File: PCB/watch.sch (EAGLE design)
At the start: 47 parts, among them IC1 ISL1209, J2 USB-MICROB, T1 BC850, U2 MKL27Z256VLH4

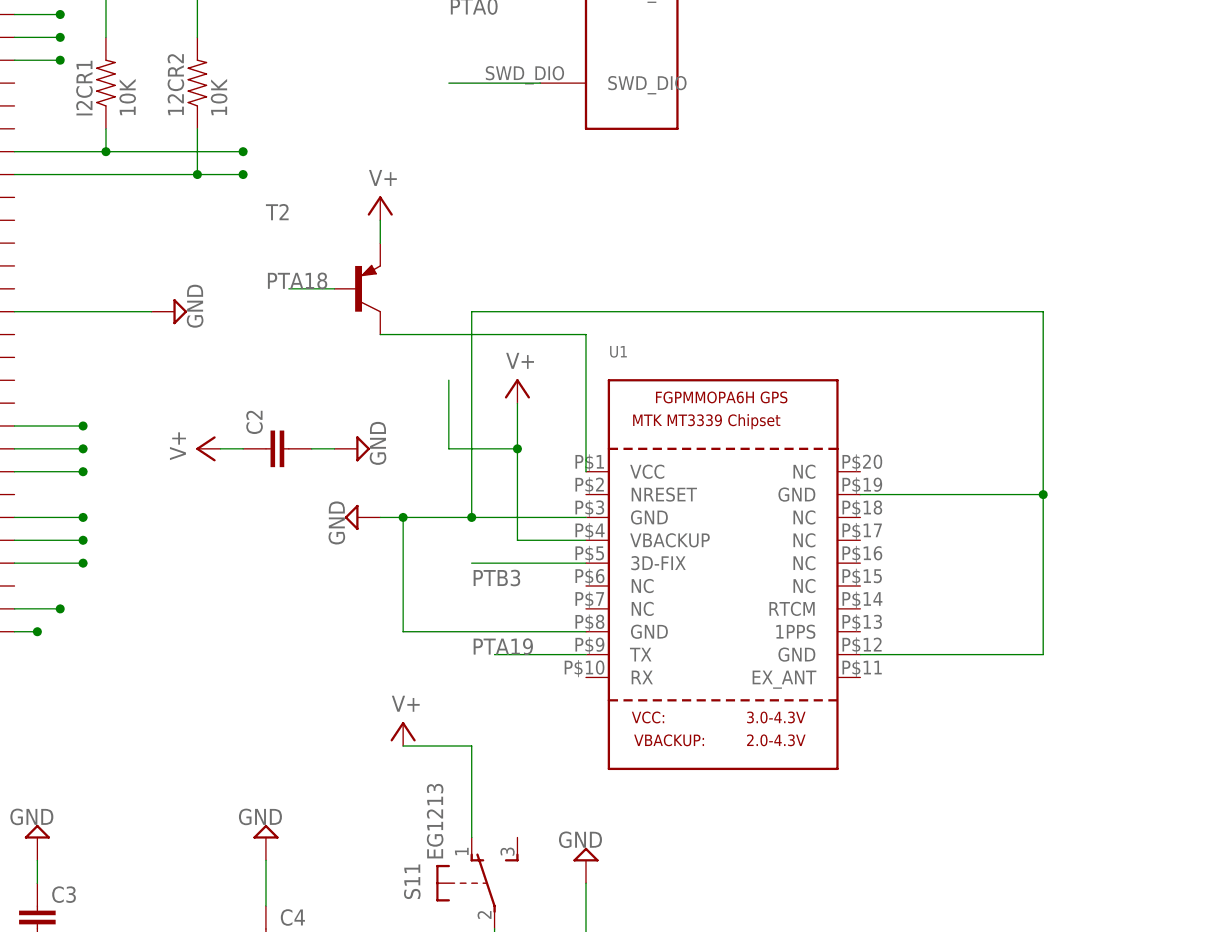
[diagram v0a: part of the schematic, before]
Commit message: cleaned up gps, added label for gps cap
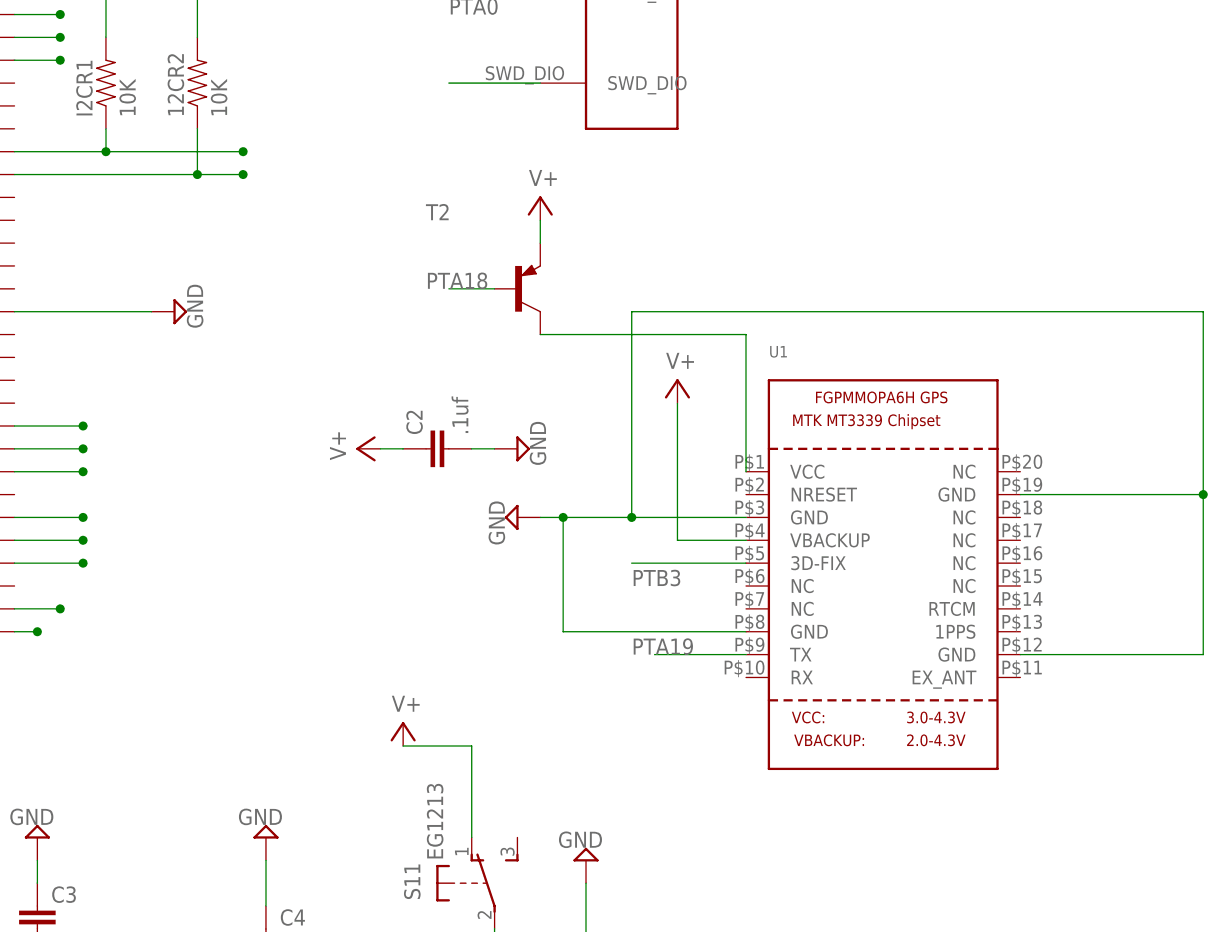
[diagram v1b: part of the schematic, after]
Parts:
- C2: value (none) -> .1uf
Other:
- moved on the sheet: C2, T2, U1
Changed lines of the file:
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@@
 <part name="SUPPLY6" library="supply2" deviceset="GND" device=""/>
 <part name="SUPPLY7" library="supply2" deviceset="GND" device=""/>
-<part name="C2" library="SparkFun" deviceset="CAP" device="0603"/>
+<part name="C2" library="SparkFun" deviceset="CAP" device="0603" value=".1uf"/>
 <part name="SUPPLY8" library="supply2" deviceset="V+" device=""/>
 <part name="SUPPLY9" library="supply2" deviceset="GND" device=""/>
@@
 <instance part="SUPPLY3" gate="1" x="-63.5" y="71.12"/>
 <instance part="SUPPLY4" gate="GND" x="58.42" y="55.88" rot="R90"/>
-<instance part="U1" gate="G$1" x="160.02" y="91.44"/>
-<instance part="SUPPLY5" gate="GND" x="119.38" y="96.52" rot="R270"/>
+<instance part="U1" gate="G$1" x="177.8" y="91.44"/>
+<instance part="SUPPLY5" gate="GND" x="137.16" y="96.52" rot="R270"/>
 <instance part="U2" gate="A" x="-25.4" y="162.56"/>
 <instance part="SUPPLY6" gate="GND" x="-53.34" y="86.36" rot="R270"/>
 <instance part="SUPPLY7" gate="GND" x="99.06" y="119.38" rot="R90"/>
-<instance part="C2" gate="G$1" x="111.76" y="104.14" rot="R90"/>
-<instance part="SUPPLY8" gate="1" x="101.6" y="104.14" rot="R90"/>
-<instance part="SUPPLY9" gate="GND" x="119.38" y="104.14" rot="R90"/>
-<instance part="SUPPLY10" gate="1" x="137.16" y="111.76"/>
+<instance part="C2" gate="G$1" x="129.54" y="104.14" rot="R90"/>
+<instance part="SUPPLY8" gate="1" x="119.38" y="104.14" rot="R90"/>
+<instance part="SUPPLY9" gate="GND" x="137.16" y="104.14" rot="R90"/>
+<instance part="SUPPLY10" gate="1" x="154.94" y="111.76"/>
 <instance part="U$3" gate="G$1" x="25.4" y="63.5"/>
 <instance part="SP1" gate="S1" x="-81.28" y="109.22" rot="R270"/>
@@
 <instance part="SUPPLY31" gate="GND" x="-129.54" y="165.1"/>
 <instance part="R17" gate="G$1" x="-152.4" y="177.8"/>
-<instance part="T2" gate="G$1" x="119.38" y="121.92"/>
-<instance part="SUPPLY32" gate="1" x="121.92" y="132.08"/>
+<instance part="T2" gate="G$1" x="137.16" y="121.92"/>
+<instance part="SUPPLY32" gate="1" x="139.7" y="132.08"/>
 </instances>
 <busses>
@@
 <pinref part="U1" gate="G$1" pin="GND@1"/>
 <pinref part="SUPPLY5" gate="GND" pin="GND"/>
-<wire x1="144.78" y1="96.52" x2="132.08" y2="96.52" width="0.1524" layer="91"/>
+<wire x1="162.56" y1="96.52" x2="149.86" y2="96.52" width="0.1524" layer="91"/>
 <pinref part="U1" gate="G$1" pin="GND@3"/>
-<wire x1="132.08" y1="96.52" x2="124.46" y2="96.52" width="0.1524" layer="91"/>
-<wire x1="124.46" y1="96.52" x2="121.92" y2="96.52" width="0.1524" layer="91"/>
-<wire x1="175.26" y1="81.28" x2="195.58" y2="81.28" width="0.1524" layer="91"/>
-<wire x1="195.58" y1="81.28" x2="195.58" y2="99.06" width="0.1524" layer="91"/>
-<wire x1="195.58" y1="99.06" x2="195.58" y2="119.38" width="0.1524" layer="91"/>
-<wire x1="195.58" y1="119.38" x2="132.08" y2="119.38" width="0.1524" layer="91"/>
-<wire x1="132.08" y1="119.38" x2="132.08" y2="96.52" width="0.1524" layer="91"/>
-<junction x="132.08" y="96.52"/>
+<wire x1="149.86" y1="96.52" x2="142.24" y2="96.52" width="0.1524" layer="91"/>
+<wire x1="142.24" y1="96.52" x2="139.7" y2="96.52" width="0.1524" layer="91"/>
+<wire x1="193.04" y1="81.28" x2="213.36" y2="81.28" width="0.1524" layer="91"/>
+<wire x1="213.36" y1="81.28" x2="213.36" y2="99.06" width="0.1524" layer="91"/>
+<wire x1="213.36" y1="99.06" x2="213.36" y2="119.38" width="0.1524" layer="91"/>
+<wire x1="213.36" y1="119.38" x2="149.86" y2="119.38" width="0.1524" layer="91"/>
+<wire x1="149.86" y1="119.38" x2="149.86" y2="96.52" width="0.1524" layer="91"/>
+<junction x="149.86" y="96.52"/>
 <pinref part="U1" gate="G$1" pin="GND@4"/>
-<wire x1="175.26" y1="99.06" x2="195.58" y2="99.06" width="0.1524" layer="91"/>
-<junction x="195.58" y="99.06"/>
+<wire x1="193.04" y1="99.06" x2="213.36" y2="99.06" width="0.1524" layer="91"/>
+<junction x="213.36" y="99.06"/>
 <pinref part="U1" gate="G$1" pin="GND@2"/>
-<wire x1="144.78" y1="83.82" x2="124.46" y2="83.82" width="0.1524" layer="91"/>
-<wire x1="124.46" y1="83.82" x2="124.46" y2="96.52" width="0.1524" layer="91"/>
-<junction x="124.46" y="96.52"/>
+<wire x1="162.56" y1="83.82" x2="142.24" y2="83.82" width="0.1524" layer="91"/>
+<wire x1="142.24" y1="83.82" x2="142.24" y2="96.52" width="0.1524" layer="91"/>
+<junction x="142.24" y="96.52"/>
 </segment>
 <segment>
 <pinref part="C2" gate="G$1" pin="2"/>
 <pinref part="SUPPLY9" gate="GND" pin="GND"/>
-<wire x1="114.3" y1="104.14" x2="116.84" y2="104.14" width="0.1524" layer="91"/>
+<wire x1="132.08" y1="104.14" x2="134.62" y2="104.14" width="0.1524" layer="91"/>
 </segment>
 <segment>
@@
 <pinref part="SUPPLY8" gate="1" pin="V+"/>
 <pinref part="C2" gate="G$1" pin="1"/>
-<wire x1="104.14" y1="104.14" x2="106.68" y2="104.14" width="0.1524" layer="91"/>
+<wire x1="121.92" y1="104.14" x2="124.46" y2="104.14" width="0.1524" layer="91"/>
 </segment>
 <segment>
 <pinref part="SUPPLY10" gate="1" pin="V+"/>
 <pinref part="U1" gate="G$1" pin="VBACKUP"/>
-<wire x1="144.78" y1="93.98" x2="137.16" y2="93.98" width="0.1524" layer="91"/>
-<wire x1="137.16" y1="93.98" x2="137.16" y2="104.14" width="0.1524" layer="91"/>
-<wire x1="137.16" y1="104.14" x2="137.16" y2="109.22" width="0.1524" layer="91"/>
-<wire x1="129.54" y1="111.76" x2="129.54" y2="104.14" width="0.1524" layer="91"/>
-<wire x1="129.54" y1="104.14" x2="137.16" y2="104.14" width="0.1524" layer="91"/>
-<junction x="137.16" y="104.14"/>
+<wire x1="162.56" y1="93.98" x2="154.94" y2="93.98" width="0.1524" layer="91"/>
+<wire x1="154.94" y1="93.98" x2="154.94" y2="109.22" width="0.1524" layer="91"/>
 </segment>
 <segment>
@@
 <pinref part="SUPPLY32" gate="1" pin="V+"/>
 <pinref part="T2" gate="G$1" pin="E"/>
-<wire x1="121.92" y1="129.54" x2="121.92" y2="127" width="0.1524" layer="91"/>
+<wire x1="139.7" y1="129.54" x2="139.7" y2="127" width="0.1524" layer="91"/>
 </segment>
 </net>
@@
 <segment>
 <pinref part="U1" gate="G$1" pin="TX"/>
-<wire x1="144.78" y1="81.28" x2="134.62" y2="81.28" width="0.1524" layer="91"/>
-<label x="132.08" y="81.28" size="1.778" layer="95"/>
+<wire x1="162.56" y1="81.28" x2="152.4" y2="81.28" width="0.1524" layer="91"/>
+<label x="149.86" y="81.28" size="1.778" layer="95"/>
 </segment>
 </net>
@@
 <segment>
 <pinref part="U1" gate="G$1" pin="VCC"/>
-<wire x1="144.78" y1="101.6" x2="144.78" y2="116.84" width="0.1524" layer="91"/>
-<wire x1="144.78" y1="116.84" x2="121.92" y2="116.84" width="0.1524" layer="91"/>
+<wire x1="162.56" y1="101.6" x2="162.56" y2="116.84" width="0.1524" layer="91"/>
+<wire x1="162.56" y1="116.84" x2="139.7" y2="116.84" width="0.1524" layer="91"/>
 <pinref part="T2" gate="G$1" pin="C"/>
 </segment>
@@
 <segment>
 <pinref part="U1" gate="G$1" pin="3D-FIX"/>
-<wire x1="144.78" y1="91.44" x2="132.08" y2="91.44" width="0.1524" layer="91"/>
-<label x="132.08" y="88.9" size="1.778" layer="95"/>
+<wire x1="162.56" y1="91.44" x2="149.86" y2="91.44" width="0.1524" layer="91"/>
+<label x="149.86" y="88.9" size="1.778" layer="95"/>
 </segment>
 </net>
@@
 <segment>
 <pinref part="T2" gate="G$1" pin="B"/>
-<wire x1="116.84" y1="121.92" x2="111.76" y2="121.92" width="0.1524" layer="91"/>
-<label x="109.22" y="121.92" size="1.778" layer="95"/>
-</segment>
-</net>
+<wire x1="134.62" y1="121.92" x2="129.54" y2="121.92" width="0.1524" layer="91"/>
+<label x="127" y="121.92" size="1.778" layer="95"/>
+</segment>
+</net>

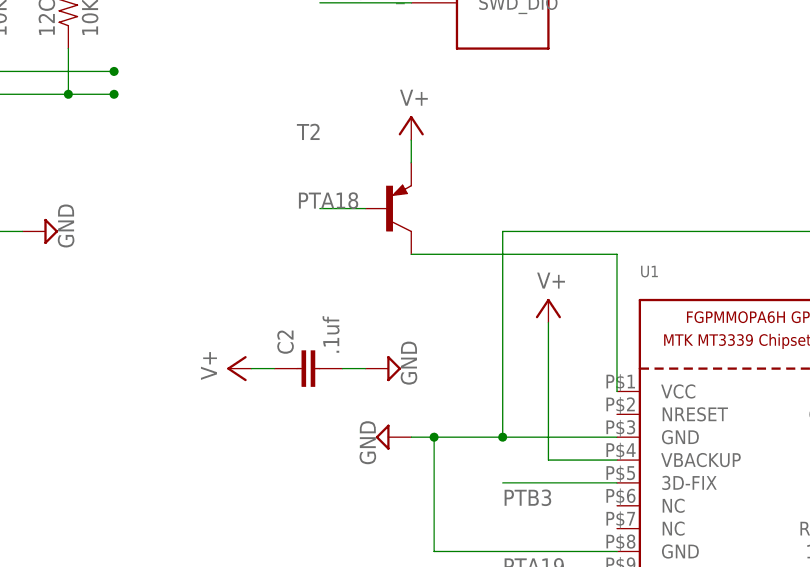
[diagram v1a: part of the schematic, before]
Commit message: added vback cap
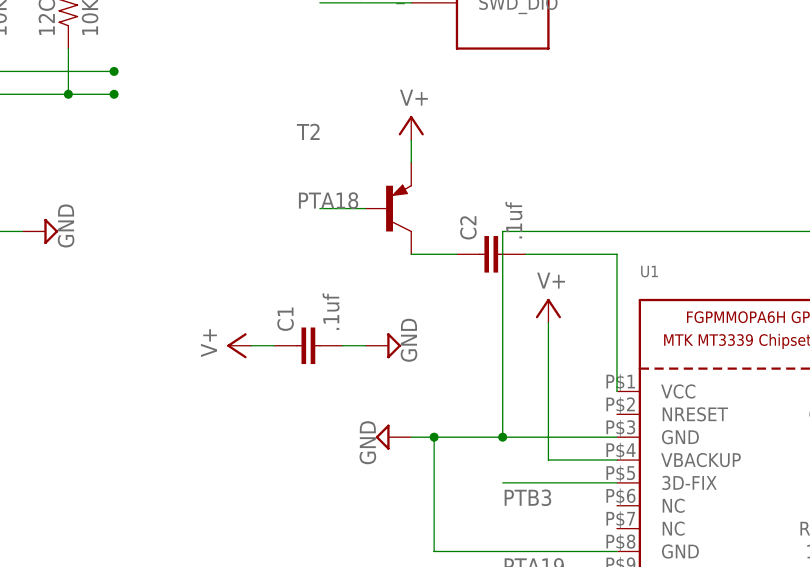
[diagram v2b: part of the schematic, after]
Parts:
- added C1: .1uf, SparkFun:CAP0603
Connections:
- new net N$2: C2.1, T2.C
- net GND: now also C1.2; no longer C2.2
- net N$6: now also C2.2; no longer T2.C
- net V+: now also C1.1; no longer C2.1
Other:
- moved on the sheet: C2
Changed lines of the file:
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@@
 <part name="SUPPLY7" library="supply2" deviceset="GND" device=""/>
 <part name="C2" library="SparkFun" deviceset="CAP" device="0603" value=".1uf"/>
-<part name="SUPPLY8" library="supply2" deviceset="V+" device=""/>
-<part name="SUPPLY9" library="supply2" deviceset="GND" device=""/>
 <part name="SUPPLY10" library="supply2" deviceset="V+" device=""/>
 <part name="U$3" library="5-wayswitch" deviceset="5-WAYSWITCH" device=""/>
@@
 <part name="T2" library="transistor" deviceset="*-PNP-" device="SOT23-EBC"/>
 <part name="SUPPLY32" library="supply2" deviceset="V+" device=""/>
+<part name="C1" library="SparkFun" deviceset="CAP" device="0603" value=".1uf"/>
+<part name="SUPPLY8" library="supply2" deviceset="V+" device=""/>
+<part name="SUPPLY9" library="supply2" deviceset="GND" device=""/>
 </parts>
 <sheets>
@@
 <instance part="SUPPLY6" gate="GND" x="-53.34" y="86.36" rot="R270"/>
 <instance part="SUPPLY7" gate="GND" x="99.06" y="119.38" rot="R90"/>
-<instance part="C2" gate="G$1" x="129.54" y="104.14" rot="R90"/>
-<instance part="SUPPLY8" gate="1" x="119.38" y="104.14" rot="R90"/>
-<instance part="SUPPLY9" gate="GND" x="137.16" y="104.14" rot="R90"/>
+<instance part="C2" gate="G$1" x="149.86" y="116.84" rot="R90"/>
 <instance part="SUPPLY10" gate="1" x="154.94" y="111.76"/>
 <instance part="U$3" gate="G$1" x="25.4" y="63.5"/>
@@
 <instance part="T2" gate="G$1" x="137.16" y="121.92"/>
 <instance part="SUPPLY32" gate="1" x="139.7" y="132.08"/>
+<instance part="C1" gate="G$1" x="129.54" y="106.68" rot="R90"/>
+<instance part="SUPPLY8" gate="1" x="119.38" y="106.68" rot="R90"/>
+<instance part="SUPPLY9" gate="GND" x="137.16" y="106.68" rot="R90"/>
 </instances>
 <busses>
@@
 </segment>
 <segment>
-<pinref part="C2" gate="G$1" pin="2"/>
-<pinref part="SUPPLY9" gate="GND" pin="GND"/>
-<wire x1="132.08" y1="104.14" x2="134.62" y2="104.14" width="0.1524" layer="91"/>
-</segment>
-<segment>
 <pinref part="SUPPLY6" gate="GND" pin="GND"/>
 <pinref part="U2" gate="A" pin="VSS_3"/>
@@
 <wire x1="-129.54" y1="172.72" x2="-129.54" y2="167.64" width="0.1524" layer="91"/>
 </segment>
+<segment>
+<pinref part="C1" gate="G$1" pin="2"/>
+<pinref part="SUPPLY9" gate="GND" pin="GND"/>
+<wire x1="132.08" y1="106.68" x2="134.62" y2="106.68" width="0.1524" layer="91"/>
+</segment>
 </net>
 <net name="V+" class="0">
@@
 <pinref part="SUPPLY3" gate="1" pin="V+"/>
 <wire x1="-63.5" y1="63.5" x2="-63.5" y2="68.58" width="0.1524" layer="91"/>
-</segment>
-<segment>
-<pinref part="SUPPLY8" gate="1" pin="V+"/>
-<pinref part="C2" gate="G$1" pin="1"/>
-<wire x1="121.92" y1="104.14" x2="124.46" y2="104.14" width="0.1524" layer="91"/>
 </segment>
 <segment>
@@
 <wire x1="139.7" y1="129.54" x2="139.7" y2="127" width="0.1524" layer="91"/>
 </segment>
+<segment>
+<pinref part="C1" gate="G$1" pin="1"/>
+<pinref part="SUPPLY8" gate="1" pin="V+"/>
+<wire x1="124.46" y1="106.68" x2="121.92" y2="106.68" width="0.1524" layer="91"/>
+</segment>
 </net>
 <net name="PTA19" class="0">
@@
 <pinref part="U1" gate="G$1" pin="VCC"/>
 <wire x1="162.56" y1="101.6" x2="162.56" y2="116.84" width="0.1524" layer="91"/>
-<wire x1="162.56" y1="116.84" x2="139.7" y2="116.84" width="0.1524" layer="91"/>
-<pinref part="T2" gate="G$1" pin="C"/>
+<pinref part="C2" gate="G$1" pin="2"/>
+<wire x1="152.4" y1="116.84" x2="162.56" y2="116.84" width="0.1524" layer="91"/>
 </segment>
 </net>
@@
 </segment>
 </net>
+<net name="N$2" class="0">
+<segment>
+<pinref part="T2" gate="G$1" pin="C"/>
+<pinref part="C2" gate="G$1" pin="1"/>
+<wire x1="139.7" y1="116.84" x2="144.78" y2="116.84" width="0.1524" layer="91"/>
+</segment>
+</net>

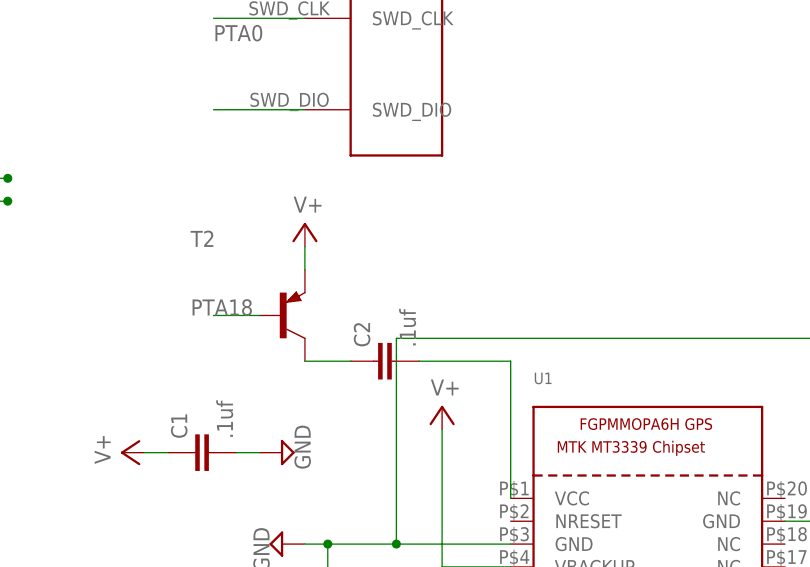
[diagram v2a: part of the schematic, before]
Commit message: fixed gps cap
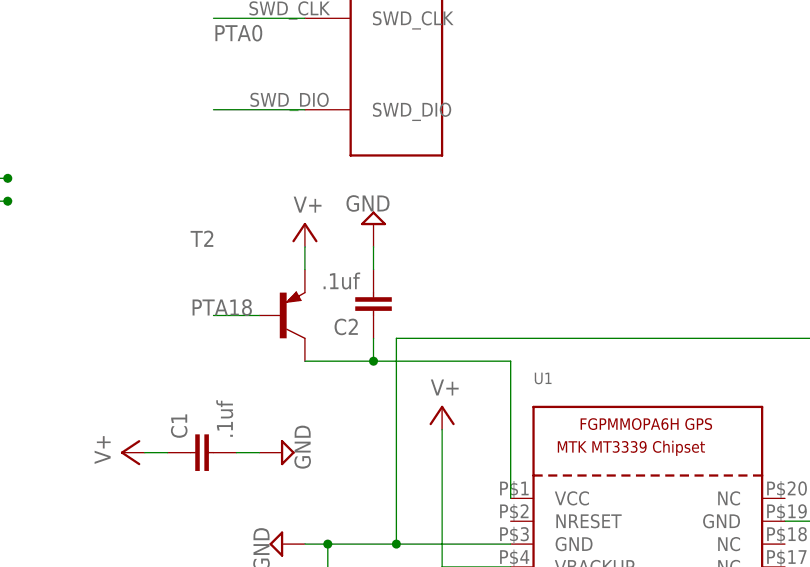
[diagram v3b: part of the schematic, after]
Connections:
- removed net N$2: C2.1, T2.C
- net GND: now also C2.2
- net N$6: now also C2.1, T2.C; no longer C2.2
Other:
- moved on the sheet: C2
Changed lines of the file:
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@@
 <part name="SUPPLY8" library="supply2" deviceset="V+" device=""/>
 <part name="SUPPLY9" library="supply2" deviceset="GND" device=""/>
+<part name="SUPPLY33" library="supply2" deviceset="GND" device=""/>
 </parts>
 <sheets>
@@
 <instance part="SUPPLY6" gate="GND" x="-53.34" y="86.36" rot="R270"/>
 <instance part="SUPPLY7" gate="GND" x="99.06" y="119.38" rot="R90"/>
-<instance part="C2" gate="G$1" x="149.86" y="116.84" rot="R90"/>
+<instance part="C2" gate="G$1" x="147.32" y="124.46" rot="R180"/>
 <instance part="SUPPLY10" gate="1" x="154.94" y="111.76"/>
 <instance part="U$3" gate="G$1" x="25.4" y="63.5"/>
@@
 <instance part="SUPPLY8" gate="1" x="119.38" y="106.68" rot="R90"/>
 <instance part="SUPPLY9" gate="GND" x="137.16" y="106.68" rot="R90"/>
+<instance part="SUPPLY33" gate="GND" x="147.32" y="132.08" rot="R180"/>
 </instances>
 <busses>
@@
 <wire x1="132.08" y1="106.68" x2="134.62" y2="106.68" width="0.1524" layer="91"/>
 </segment>
+<segment>
+<pinref part="C2" gate="G$1" pin="2"/>
+<pinref part="SUPPLY33" gate="GND" pin="GND"/>
+<wire x1="147.32" y1="127" x2="147.32" y2="129.54" width="0.1524" layer="91"/>
+</segment>
 </net>
 <net name="V+" class="0">
@@
 <pinref part="U1" gate="G$1" pin="VCC"/>
 <wire x1="162.56" y1="101.6" x2="162.56" y2="116.84" width="0.1524" layer="91"/>
-<pinref part="C2" gate="G$1" pin="2"/>
-<wire x1="152.4" y1="116.84" x2="162.56" y2="116.84" width="0.1524" layer="91"/>
+<pinref part="T2" gate="G$1" pin="C"/>
+<wire x1="162.56" y1="116.84" x2="147.32" y2="116.84" width="0.1524" layer="91"/>
+<pinref part="C2" gate="G$1" pin="1"/>
+<wire x1="147.32" y1="116.84" x2="139.7" y2="116.84" width="0.1524" layer="91"/>
+<wire x1="147.32" y1="116.84" x2="147.32" y2="119.38" width="0.1524" layer="91"/>
+<junction x="147.32" y="116.84"/>
 </segment>
 </net>
@@
 </segment>
 </net>
-<net name="N$2" class="0">
-<segment>
-<pinref part="T2" gate="G$1" pin="C"/>
-<pinref part="C2" gate="G$1" pin="1"/>
-<wire x1="139.7" y1="116.84" x2="144.78" y2="116.84" width="0.1524" layer="91"/>
-</segment>
-</net>
